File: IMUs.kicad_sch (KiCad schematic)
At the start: 8 parts, among them U301 BMP390, U302 LSM6DSL, U303 MLX90394RLD-AAA-000-SP

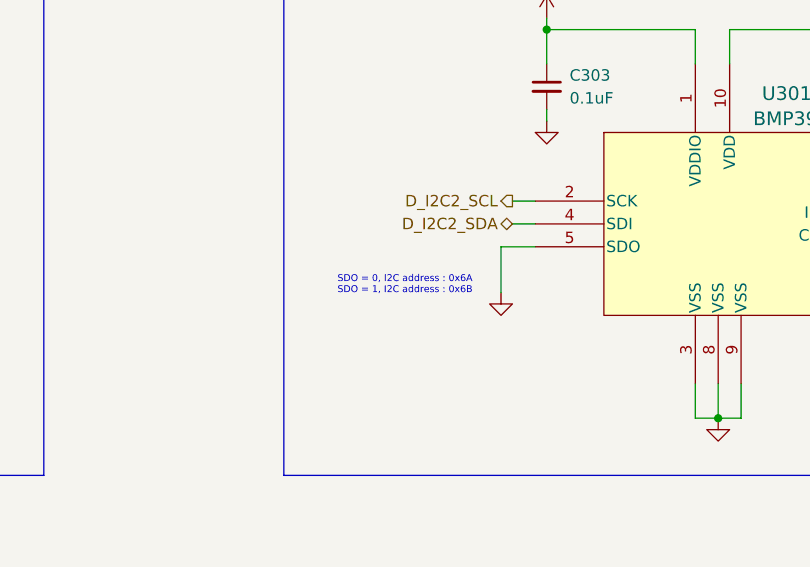
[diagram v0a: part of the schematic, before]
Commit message: fix: barometer I2C address
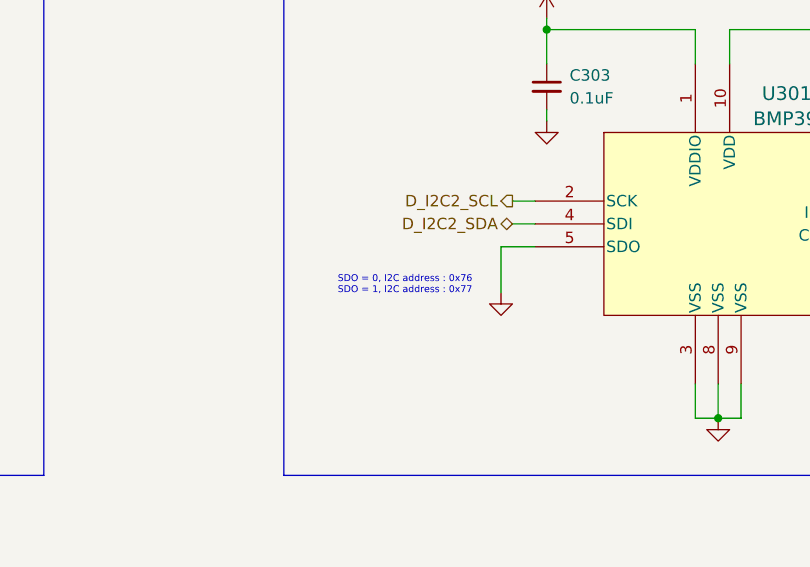
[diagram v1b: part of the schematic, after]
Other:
- note added: "SDO = 0, I2C address : 0x76 SDO = 1, I2C address : 0x77"
- note removed: "SDO = 0, I2C address : 0x6A SDO = 1, I2C address : 0x6B"
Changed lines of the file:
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@@
 		)
 	)
-	(text "SDO = 0, I2C address : 0x6A\nSDO = 1, I2C address : 0x6B"
+	(text "SDO = 0, I2C address : 0x76\nSDO = 1, I2C address : 0x77"
 		(exclude_from_sim no)
 		(at 172.212 86.868 0)
